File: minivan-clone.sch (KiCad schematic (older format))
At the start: 21 parts, among them CON101 HRO-TYPE-C-31-M-12, SW101 SW_PUSH, U101 ATMEGA32U2, X101 XTAL_GND

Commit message: done with tracks for leftmost cols
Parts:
- D202: symbol minivan-clone-rescue:PRTR5V0U2X-Power_Protection -> minivan-clone-rescue:PRTR5V0U2X-Power_Protection-minivan-clone-rescue
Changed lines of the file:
@@
 Text Label 2750 5300 0    50   ~ 0
 PD3
-Text Label 2750 5200 0    50   ~ 0
-PD4
+Text Label 2750 6000 0    50   ~ 0
+PD5
+Text Label 2750 5900 0    50   ~ 0
+PD6
+Text Label 2750 5800 0    50   ~ 0
+PB0
+Text Label 2750 4700 0    50   ~ 0
+PB5
+Text Label 2750 4600 0    50   ~ 0
+PB6
 Text Label 2750 5100 0    50   ~ 0
-PD5
-Text Label 2750 4500 0    50   ~ 0
-PD6
-Text Label 2750 4600 0    50   ~ 0
-PB0
+PB7
 Text Label 2750 5700 0    50   ~ 0
-PB5
-Text Label 2750 5800 0    50   ~ 0
-PB6
-Text Label 2750 6000 0    50   ~ 0
-PB7
-Text Label 2750 6100 0    50   ~ 0
-PC4
-Text Label 2750 4700 0    50   ~ 0
 PB1
 Text Label 2750 4900 0    50   ~ 0
@@
 	7350 5900 8150 5900
 $Comp
-L minivan-clone-rescue:GND-power #PWR0101
+L minivan-clone-rescue:GND-power-minivan-clone-rescue #PWR0101
 U 1 1 5D783424
 P 9900 1150
@@
 $EndComp
 $Comp
-L minivan-clone-rescue:GND-power #PWR0103
+L minivan-clone-rescue:GND-power-minivan-clone-rescue #PWR0103
 U 1 1 5D783D84
 P 11050 2000
@@
 $EndComp
 $Comp
-L minivan-clone-rescue:GND-power #PWR0104
+L minivan-clone-rescue:GND-power-minivan-clone-rescue #PWR0104
 U 1 1 5D7843A4
 P 10300 2350
@@
 $EndComp
 $Comp
-L minivan-clone-rescue:GND-power #PWR0105
+L minivan-clone-rescue:GND-power-minivan-clone-rescue #PWR0105
 U 1 1 5D784B88
 P 5850 2750
@@
 $EndComp
 $Comp
-L minivan-clone-rescue:GND-power #PWR0106
+L minivan-clone-rescue:GND-power-minivan-clone-rescue #PWR0106
 U 1 1 5D784E14
 P 6850 1250
@@
 $EndComp
 $Comp
-L minivan-clone-rescue:GND-power #PWR0107
+L minivan-clone-rescue:GND-power-minivan-clone-rescue #PWR0107
 U 1 1 5D785521
 P 5350 1800
@@
 $EndComp
 $Comp
-L minivan-clone-rescue:GND-power #PWR0108
+L minivan-clone-rescue:GND-power-minivan-clone-rescue #PWR0108
 U 1 1 5D7857C7
 P 4750 1800
@@
 Connection ~ 4750 1800
 $Comp
-L minivan-clone-rescue:GND-power #PWR0109
+L minivan-clone-rescue:GND-power-minivan-clone-rescue #PWR0109
 U 1 1 5D785DFD
 P 1950 1550
@@
 $EndComp
 $Comp
-L minivan-clone-rescue:GND-power #PWR0110
+L minivan-clone-rescue:GND-power-minivan-clone-rescue #PWR0110
 U 1 1 5D7865E1
 P 1950 2750
@@
 Connection ~ 1950 2750
 $Comp
-L minivan-clone-rescue:GND-power #PWR0111
+L minivan-clone-rescue:GND-power-minivan-clone-rescue #PWR0111
 U 1 1 5D78689D
 P 2500 3100
@@
 	2500 3100 2700 3100
 $Comp
-L minivan-clone-rescue:GND-power #PWR0112
+L minivan-clone-rescue:GND-power-minivan-clone-rescue #PWR0112
 U 1 1 5D786B67
 P 8150 5900
@@
 	8150 5900 8500 5900
 $Comp
-L minivan-clone-rescue:PRTR5V0U2X-Power_Protection D202
+L minivan-clone-rescue:PRTR5V0U2X-Power_Protection-minivan-clone-rescue D202
 U 1 1 5D787265
 P 5250 4000
@@
 $EndComp
 $Comp
-L minivan-clone-rescue:GND-power #PWR0113
+L minivan-clone-rescue:GND-power-minivan-clone-rescue #PWR0113
 U 1 1 5D7884C0
 P 5250 4500
@@
 pre_D+
 $Comp
-L minivan-clone-rescue:+5V-power #PWR0102
+L minivan-clone-rescue:+5V-power-minivan-clone-rescue #PWR0102
 U 1 1 5D78AA14
 P 5250 3500
@@
 $EndComp
 $Comp
-L minivan-clone-rescue:+5V-power #PWR0114
+L minivan-clone-rescue:+5V-power-minivan-clone-rescue #PWR0114
 U 1 1 5D78B5BE
 P 3000 1650
@@
 $EndComp
 $Comp
-L minivan-clone-rescue:+5V-power #PWR0115
+L minivan-clone-rescue:+5V-power-minivan-clone-rescue #PWR0115
 U 1 1 5D78C361
 P 6850 1350
@@
 $EndComp
 $Comp
-L minivan-clone-rescue:+5V-power #PWR0116
+L minivan-clone-rescue:+5V-power-minivan-clone-rescue #PWR0116
 U 1 1 5D78C75A
 P 9000 1050
@@
 Connection ~ 9000 1050
 $Comp
-L minivan-clone-rescue:GND-power #PWR0117
+L minivan-clone-rescue:GND-power-minivan-clone-rescue #PWR0117
 U 1 1 5D792811
 P 9000 1450
@@
 $EndComp
 $Comp
-L minivan-clone-rescue:+5V-power #PWR0118
+L minivan-clone-rescue:+5V-power-minivan-clone-rescue #PWR0118
 U 1 1 5D792F03
 P 10300 1300
@@
 $EndComp
 $Comp
-L minivan-clone-rescue:+5V-power #PWR0119
+L minivan-clone-rescue:+5V-power-minivan-clone-rescue #PWR0119
 U 1 1 5D793283
 P 8150 5500
@@
 Text Label 2750 5600 0    50   ~ 0
 PB2
-Text Label 2750 5900 0    50   ~ 0
+Text Label 2750 4500 0    50   ~ 0
 PC6
+Text Label 2750 5200 0    50   ~ 0
+PC4
+Text Label 2750 6100 0    50   ~ 0
+PD4
 Text Label 2750 5000 0    50   ~ 0
 PB4

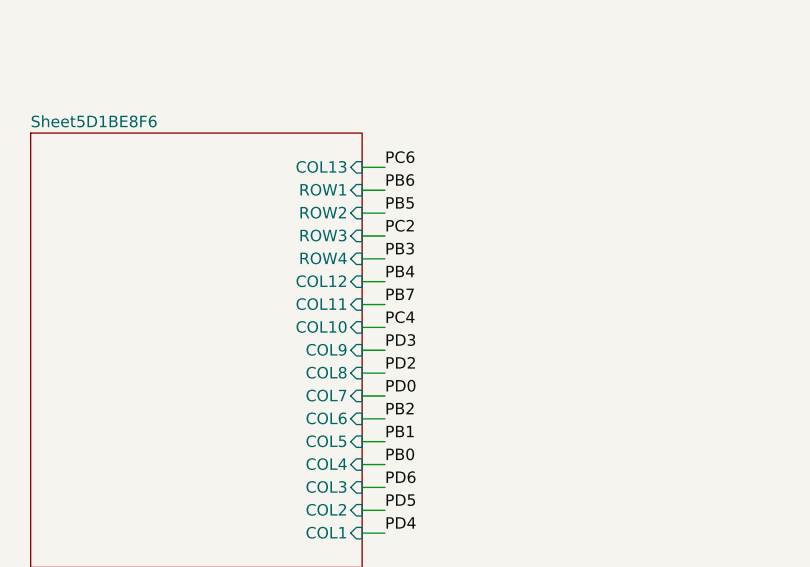
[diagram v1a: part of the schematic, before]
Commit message: tracks for all leftmost rows, started with rightmost cols
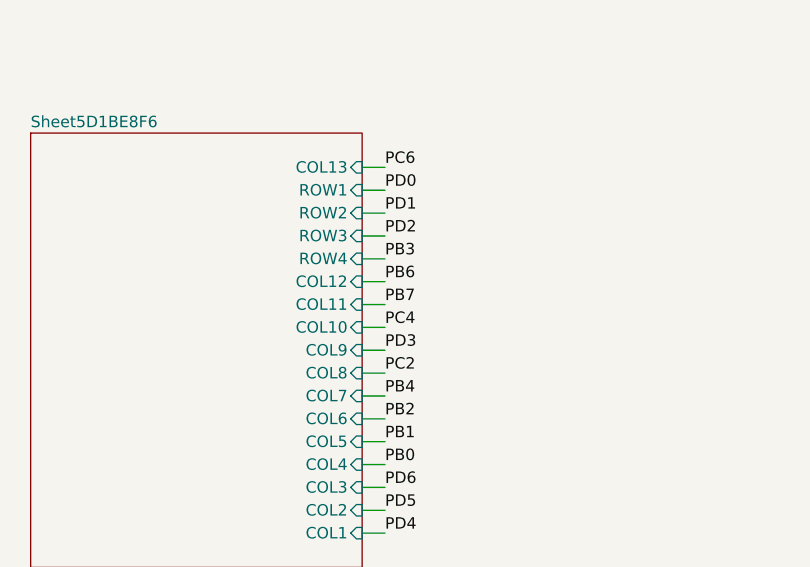
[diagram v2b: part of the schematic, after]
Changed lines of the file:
@@
 	1    0    0    -1
 $EndComp
-Text Label 2750 4800 0    50   ~ 0
+Text Label 2750 5400 0    50   ~ 0
 PC2
-Text Label 2750 5500 0    50   ~ 0
+Text Label 2750 4600 0    50   ~ 0
 PD0
 Text Label 2750 5300 0    50   ~ 0
 PD3
-Text Label 2750 6000 0    50   ~ 0
-PD5
 Text Label 2750 5900 0    50   ~ 0
 PD6
@@
 PB0
 Text Label 2750 4700 0    50   ~ 0
-PB5
-Text Label 2750 4600 0    50   ~ 0
-PB6
+PD1
 Text Label 2750 5100 0    50   ~ 0
 PB7
@@
 Text Label 2750 4900 0    50   ~ 0
 PB3
-Text Label 2750 5400 0    50   ~ 0
+Text Label 2750 4800 0    50   ~ 0
 PD2
 Wire Wire Line
@@
 Text Label 2750 6100 0    50   ~ 0
 PD4
+Text Label 2750 5500 0    50   ~ 0
+PB4
+Text Label 2750 6000 0    50   ~ 0
+PD5
 Text Label 2750 5000 0    50   ~ 0
-PB4
+PB6
 $EndSCHEMATC

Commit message: added all tracks
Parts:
- D202: symbol minivan-clone-rescue:PRTR5V0U2X-Power_Protection-minivan-clone-rescue -> minivan-clone-rescue:PRTR5V0U2X-Power_Protection-minivan-clone-rescue-minivan-clone-rescue
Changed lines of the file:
@@
 	1    0    0    -1
 $EndComp
-Text Label 2750 5400 0    50   ~ 0
-PC2
+Text Label 2750 5200 0    50   ~ 0
+PC5
 Text Label 2750 4600 0    50   ~ 0
 PD0
-Text Label 2750 5300 0    50   ~ 0
-PD3
+Text Label 2750 5000 0    50   ~ 0
+PC6
 Text Label 2750 5900 0    50   ~ 0
 PD6
@@
 PD1
 Text Label 2750 5100 0    50   ~ 0
-PB7
+PC4
 Text Label 2750 5700 0    50   ~ 0
 PB1
@@
 	7350 5900 8150 5900
 $Comp
-L minivan-clone-rescue:GND-power-minivan-clone-rescue #PWR0101
+L minivan-clone-rescue:GND-power-minivan-clone-rescue-minivan-clone-rescue #PWR0101
 U 1 1 5D783424
 P 9900 1150
@@
 $EndComp
 $Comp
-L minivan-clone-rescue:GND-power-minivan-clone-rescue #PWR0103
+L minivan-clone-rescue:GND-power-minivan-clone-rescue-minivan-clone-rescue #PWR0103
 U 1 1 5D783D84
 P 11050 2000
@@
 $EndComp
 $Comp
-L minivan-clone-rescue:GND-power-minivan-clone-rescue #PWR0104
+L minivan-clone-rescue:GND-power-minivan-clone-rescue-minivan-clone-rescue #PWR0104
 U 1 1 5D7843A4
 P 10300 2350
@@
 $EndComp
 $Comp
-L minivan-clone-rescue:GND-power-minivan-clone-rescue #PWR0105
+L minivan-clone-rescue:GND-power-minivan-clone-rescue-minivan-clone-rescue #PWR0105
 U 1 1 5D784B88
 P 5850 2750
@@
 $EndComp
 $Comp
-L minivan-clone-rescue:GND-power-minivan-clone-rescue #PWR0106
+L minivan-clone-rescue:GND-power-minivan-clone-rescue-minivan-clone-rescue #PWR0106
 U 1 1 5D784E14
 P 6850 1250
@@
 $EndComp
 $Comp
-L minivan-clone-rescue:GND-power-minivan-clone-rescue #PWR0107
+L minivan-clone-rescue:GND-power-minivan-clone-rescue-minivan-clone-rescue #PWR0107
 U 1 1 5D785521
 P 5350 1800
@@
 $EndComp
 $Comp
-L minivan-clone-rescue:GND-power-minivan-clone-rescue #PWR0108
+L minivan-clone-rescue:GND-power-minivan-clone-rescue-minivan-clone-rescue #PWR0108
 U 1 1 5D7857C7
 P 4750 1800
@@
 Connection ~ 4750 1800
 $Comp
-L minivan-clone-rescue:GND-power-minivan-clone-rescue #PWR0109
+L minivan-clone-rescue:GND-power-minivan-clone-rescue-minivan-clone-rescue #PWR0109
 U 1 1 5D785DFD
 P 1950 1550
@@
 $EndComp
 $Comp
-L minivan-clone-rescue:GND-power-minivan-clone-rescue #PWR0110
+L minivan-clone-rescue:GND-power-minivan-clone-rescue-minivan-clone-rescue #PWR0110
 U 1 1 5D7865E1
 P 1950 2750
@@
 Connection ~ 1950 2750
 $Comp
-L minivan-clone-rescue:GND-power-minivan-clone-rescue #PWR0111
+L minivan-clone-rescue:GND-power-minivan-clone-rescue-minivan-clone-rescue #PWR0111
 U 1 1 5D78689D
 P 2500 3100
@@
 	2500 3100 2700 3100
 $Comp
-L minivan-clone-rescue:GND-power-minivan-clone-rescue #PWR0112
+L minivan-clone-rescue:GND-power-minivan-clone-rescue-minivan-clone-rescue #PWR0112
 U 1 1 5D786B67
 P 8150 5900
@@
 	8150 5900 8500 5900
 $Comp
-L minivan-clone-rescue:PRTR5V0U2X-Power_Protection-minivan-clone-rescue D202
+L minivan-clone-rescue:PRTR5V0U2X-Power_Protection-minivan-clone-rescue-minivan-clone-rescue D202
 U 1 1 5D787265
 P 5250 4000
@@
 $EndComp
 $Comp
-L minivan-clone-rescue:GND-power-minivan-clone-rescue #PWR0113
+L minivan-clone-rescue:GND-power-minivan-clone-rescue-minivan-clone-rescue #PWR0113
 U 1 1 5D7884C0
 P 5250 4500
@@
 pre_D+
 $Comp
-L minivan-clone-rescue:+5V-power-minivan-clone-rescue #PWR0102
+L minivan-clone-rescue:+5V-power-minivan-clone-rescue-minivan-clone-rescue #PWR0102
 U 1 1 5D78AA14
 P 5250 3500
@@
 $EndComp
 $Comp
-L minivan-clone-rescue:+5V-power-minivan-clone-rescue #PWR0114
+L minivan-clone-rescue:+5V-power-minivan-clone-rescue-minivan-clone-rescue #PWR0114
 U 1 1 5D78B5BE
 P 3000 1650
@@
 $EndComp
 $Comp
-L minivan-clone-rescue:+5V-power-minivan-clone-rescue #PWR0115
+L minivan-clone-rescue:+5V-power-minivan-clone-rescue-minivan-clone-rescue #PWR0115
 U 1 1 5D78C361
 P 6850 1350
@@
 $EndComp
 $Comp
-L minivan-clone-rescue:+5V-power-minivan-clone-rescue #PWR0116
+L minivan-clone-rescue:+5V-power-minivan-clone-rescue-minivan-clone-rescue #PWR0116
 U 1 1 5D78C75A
 P 9000 1050
@@
 Connection ~ 9000 1050
 $Comp
-L minivan-clone-rescue:GND-power-minivan-clone-rescue #PWR0117
+L minivan-clone-rescue:GND-power-minivan-clone-rescue-minivan-clone-rescue #PWR0117
 U 1 1 5D792811
 P 9000 1450
@@
 $EndComp
 $Comp
-L minivan-clone-rescue:+5V-power-minivan-clone-rescue #PWR0118
+L minivan-clone-rescue:+5V-power-minivan-clone-rescue-minivan-clone-rescue #PWR0118
 U 1 1 5D792F03
 P 10300 1300
@@
 $EndComp
 $Comp
-L minivan-clone-rescue:+5V-power-minivan-clone-rescue #PWR0119
+L minivan-clone-rescue:+5V-power-minivan-clone-rescue-minivan-clone-rescue #PWR0119
 U 1 1 5D793283
 P 8150 5500
@@
 PB2
 Text Label 2750 4500 0    50   ~ 0
-PC6
-Text Label 2750 5200 0    50   ~ 0
-PC4
+PC7
+Text Label 2750 5400 0    50   ~ 0
+PB5
 Text Label 2750 6100 0    50   ~ 0
 PD4
@@
 Text Label 2750 6000 0    50   ~ 0
 PD5
-Text Label 2750 5000 0    50   ~ 0
+Text Label 2750 5300 0    50   ~ 0
 PB6
 $EndSCHEMATC

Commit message: swapped incorrect - and + for usb
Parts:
- CON101: symbol minivan-clone-rescue:HRO-TYPE-C-31-M-12-Type-C-minivan-clone-rescue-minivan-clone-rescue -> minivan-clone-rescue:HRO-TYPE-C-31-M-12-Type-C-minivan-clone-rescue-minivan-clone-rescue-minivan-clone-rescue
- D202: symbol minivan-clone-rescue:PRTR5V0U2X-Power_Protection-minivan-clone-rescue-minivan-clone-rescue -> minivan-clone-rescue:PRTR5V0U2X-Power_Protection-minivan-clone-rescue-minivan-clone-rescue-minivan-clone-rescue
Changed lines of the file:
@@
 EESchema Schematic File Version 4
-LIBS:minivan-clone-cache
 EELAYER 30 0
 EELAYER END
@@
 	2200 2250 1950 2250
 Text Label 3900 1950 0    50   ~ 0
+D-
+Text Label 3950 2050 0    50   ~ 0
 D+
-Text Label 3950 2050 0    50   ~ 0
-D-
 Wire Wire Line
 	1950 2550 2500 2550
@@
 	1950 2750 1950 2650
 $Comp
-L minivan-clone-rescue:HRO-TYPE-C-31-M-12-Type-C-minivan-clone-rescue-minivan-clone-rescue CON101
+L minivan-clone-rescue:HRO-TYPE-C-31-M-12-Type-C-minivan-clone-rescue-minivan-clone-rescue-minivan-clone-rescue CON101
 U 1 1 5D1BD550
 P 1850 2100
@@
 	7350 5900 8150 5900
 $Comp
-L minivan-clone-rescue:GND-power-minivan-clone-rescue-minivan-clone-rescue #PWR0101
+L minivan-clone-rescue:GND-power-minivan-clone-rescue-minivan-clone-rescue-minivan-clone-rescue #PWR0101
 U 1 1 5D783424
 P 9900 1150
@@
 $EndComp
 $Comp
-L minivan-clone-rescue:GND-power-minivan-clone-rescue-minivan-clone-rescue #PWR0103
+L minivan-clone-rescue:GND-power-minivan-clone-rescue-minivan-clone-rescue-minivan-clone-rescue #PWR0103
 U 1 1 5D783D84
 P 11050 2000
@@
 $EndComp
 $Comp
-L minivan-clone-rescue:GND-power-minivan-clone-rescue-minivan-clone-rescue #PWR0104
+L minivan-clone-rescue:GND-power-minivan-clone-rescue-minivan-clone-rescue-minivan-clone-rescue #PWR0104
 U 1 1 5D7843A4
 P 10300 2350
@@
 $EndComp
 $Comp
-L minivan-clone-rescue:GND-power-minivan-clone-rescue-minivan-clone-rescue #PWR0105
+L minivan-clone-rescue:GND-power-minivan-clone-rescue-minivan-clone-rescue-minivan-clone-rescue #PWR0105
 U 1 1 5D784B88
 P 5850 2750
@@
 $EndComp
 $Comp
-L minivan-clone-rescue:GND-power-minivan-clone-rescue-minivan-clone-rescue #PWR0106
+L minivan-clone-rescue:GND-power-minivan-clone-rescue-minivan-clone-rescue-minivan-clone-rescue #PWR0106
 U 1 1 5D784E14
 P 6850 1250
@@
 $EndComp
 $Comp
-L minivan-clone-rescue:GND-power-minivan-clone-rescue-minivan-clone-rescue #PWR0107
+L minivan-clone-rescue:GND-power-minivan-clone-rescue-minivan-clone-rescue-minivan-clone-rescue #PWR0107
 U 1 1 5D785521
 P 5350 1800
@@
 $EndComp
 $Comp
-L minivan-clone-rescue:GND-power-minivan-clone-rescue-minivan-clone-rescue #PWR0108
+L minivan-clone-rescue:GND-power-minivan-clone-rescue-minivan-clone-rescue-minivan-clone-rescue #PWR0108
 U 1 1 5D7857C7
 P 4750 1800
@@
 Connection ~ 4750 1800
 $Comp
-L minivan-clone-rescue:GND-power-minivan-clone-rescue-minivan-clone-rescue #PWR0109
+L minivan-clone-rescue:GND-power-minivan-clone-rescue-minivan-clone-rescue-minivan-clone-rescue #PWR0109
 U 1 1 5D785DFD
 P 1950 1550
@@
 $EndComp
 $Comp
-L minivan-clone-rescue:GND-power-minivan-clone-rescue-minivan-clone-rescue #PWR0110
+L minivan-clone-rescue:GND-power-minivan-clone-rescue-minivan-clone-rescue-minivan-clone-rescue #PWR0110
 U 1 1 5D7865E1
 P 1950 2750
@@
 Connection ~ 1950 2750
 $Comp
-L minivan-clone-rescue:GND-power-minivan-clone-rescue-minivan-clone-rescue #PWR0111
+L minivan-clone-rescue:GND-power-minivan-clone-rescue-minivan-clone-rescue-minivan-clone-rescue #PWR0111
 U 1 1 5D78689D
 P 2500 3100
@@
 	2500 3100 2700 3100
 $Comp
-L minivan-clone-rescue:GND-power-minivan-clone-rescue-minivan-clone-rescue #PWR0112
+L minivan-clone-rescue:GND-power-minivan-clone-rescue-minivan-clone-rescue-minivan-clone-rescue #PWR0112
 U 1 1 5D786B67
 P 8150 5900
@@
 	8150 5900 8500 5900
 $Comp
-L minivan-clone-rescue:PRTR5V0U2X-Power_Protection-minivan-clone-rescue-minivan-clone-rescue D202
+L minivan-clone-rescue:PRTR5V0U2X-Power_Protection-minivan-clone-rescue-minivan-clone-rescue-minivan-clone-rescue D202
 U 1 1 5D787265
 P 5250 4000
@@
 $EndComp
 $Comp
-L minivan-clone-rescue:GND-power-minivan-clone-rescue-minivan-clone-rescue #PWR0113
+L minivan-clone-rescue:GND-power-minivan-clone-rescue-minivan-clone-rescue-minivan-clone-rescue #PWR0113
 U 1 1 5D7884C0
 P 5250 4500
@@
 pre_D+
 $Comp
-L minivan-clone-rescue:+5V-power-minivan-clone-rescue-minivan-clone-rescue #PWR0102
+L minivan-clone-rescue:+5V-power-minivan-clone-rescue-minivan-clone-rescue-minivan-clone-rescue #PWR0102
 U 1 1 5D78AA14
 P 5250 3500
@@
 $EndComp
 $Comp
-L minivan-clone-rescue:+5V-power-minivan-clone-rescue-minivan-clone-rescue #PWR0114
+L minivan-clone-rescue:+5V-power-minivan-clone-rescue-minivan-clone-rescue-minivan-clone-rescue #PWR0114
 U 1 1 5D78B5BE
 P 3000 1650
@@
 $EndComp
 $Comp
-L minivan-clone-rescue:+5V-power-minivan-clone-rescue-minivan-clone-rescue #PWR0115
+L minivan-clone-rescue:+5V-power-minivan-clone-rescue-minivan-clone-rescue-minivan-clone-rescue #PWR0115
 U 1 1 5D78C361
 P 6850 1350
@@
 $EndComp
 $Comp
-L minivan-clone-rescue:+5V-power-minivan-clone-rescue-minivan-clone-rescue #PWR0116
+L minivan-clone-rescue:+5V-power-minivan-clone-rescue-minivan-clone-rescue-minivan-clone-rescue #PWR0116
 U 1 1 5D78C75A
 P 9000 1050
@@
 Connection ~ 9000 1050
 $Comp
-L minivan-clone-rescue:GND-power-minivan-clone-rescue-minivan-clone-rescue #PWR0117
+L minivan-clone-rescue:GND-power-minivan-clone-rescue-minivan-clone-rescue-minivan-clone-rescue #PWR0117
 U 1 1 5D792811
 P 9000 1450
@@
 $EndComp
 $Comp
-L minivan-clone-rescue:+5V-power-minivan-clone-rescue-minivan-clone-rescue #PWR0118
+L minivan-clone-rescue:+5V-power-minivan-clone-rescue-minivan-clone-rescue-minivan-clone-rescue #PWR0118
 U 1 1 5D792F03
 P 10300 1300
@@
 $EndComp
 $Comp
-L minivan-clone-rescue:+5V-power-minivan-clone-rescue-minivan-clone-rescue #PWR0119
+L minivan-clone-rescue:+5V-power-minivan-clone-rescue-minivan-clone-rescue-minivan-clone-rescue #PWR0119
 U 1 1 5D793283
 P 8150 5500
@@
 	8150 5500 8500 5500
 Text Label 2600 2050 0    50   ~ 0
+pre_D+
+Text Label 2600 1950 0    50   ~ 0
 pre_D-
-Text Label 2600 1950 0    50   ~ 0
-pre_D+
 Wire Wire Line
 	2650 5400 2750 5400
